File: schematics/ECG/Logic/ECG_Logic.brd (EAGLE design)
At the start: 29.6 x 27.7 mm, 77 parts, among them IC1 ADS1293, IC2 LIS3DH, IC3 MCP1703, IC4 CC2541, IC5 FSA4157, IC6 FSA4157, IC7 FSA4157, P1 TARGET_RA, P2 TARGET_RA, P3 TARGET_RA, P4 TARGET_RA, P5 TARGET_RA, P6 TARGET_RA, P7 TARGET_RA, X1 XTAL-2SMD, X2 XTAL_403, X3 ECS-40-20-4VX

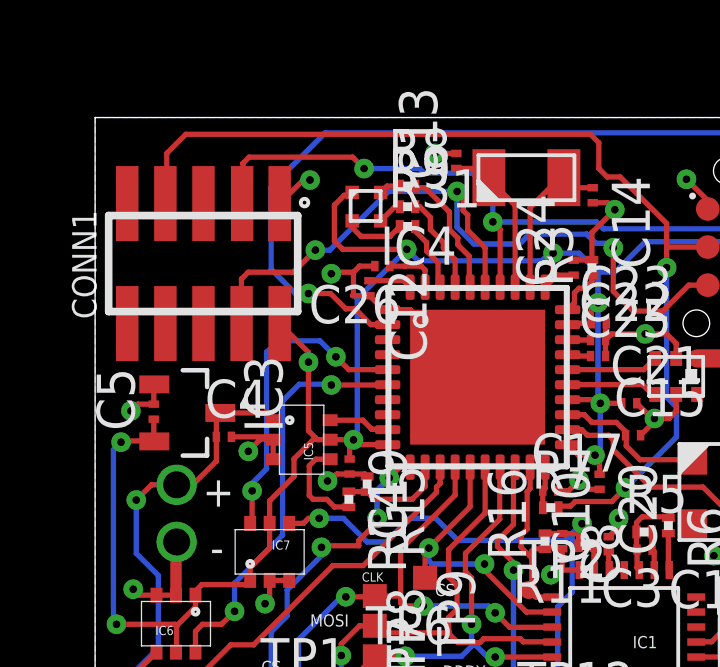
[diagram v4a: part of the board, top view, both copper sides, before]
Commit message: board only gets power when external accessory is plugged into it
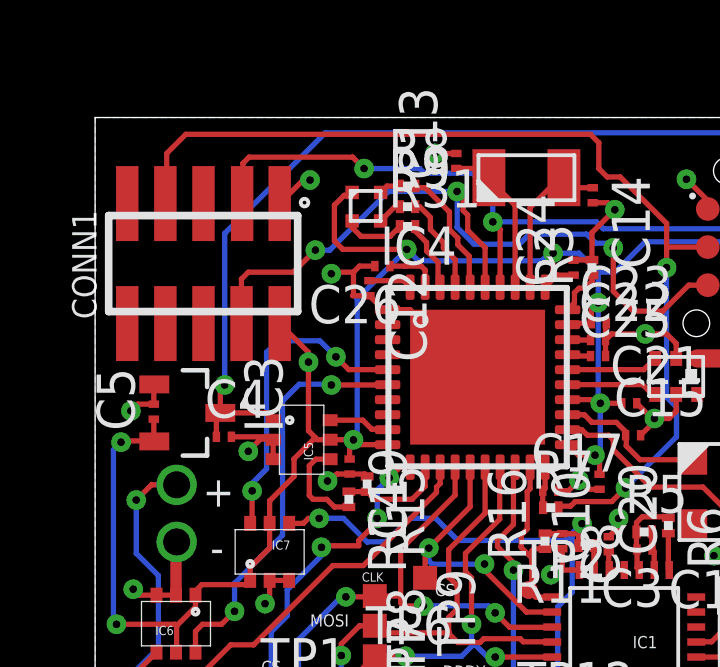
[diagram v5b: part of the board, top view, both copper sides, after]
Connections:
- removed net BOARD_DETECT: IC4.2, P7.1
- new net BATT_DETECT: C4.1, IC3.3, IC5.1, P7.1
- net BATT: no longer C4.1, IC3.3, IC5.1
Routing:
- net BATT_DETECT: track 0.00 -> 30.3 mm, vias 0 -> 1
- net BOARD_DETECT: track 26.8 -> 0.00 mm, vias 1 -> 0
- net BATT: track 44.2 -> 39.1 mm
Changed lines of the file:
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@@
 <?xml version="1.0" encoding="utf-8"?>
 <!DOCTYPE eagle SYSTEM "eagle.dtd">
-<eagle version="6.5.0">
+<eagle version="6.4">
 <drawing>
 <settings>
@@
 </signal>
 <signal name="BATT">
-<contactref element="IC5" pad="1"/>
-<contactref element="IC3" pad="3"/>
-<contactref element="C4" pad="1"/>
-<wire x1="4.1726" y1="17.8396" x2="5.6912" y2="17.8396" width="0.1778" layer="1"/>
-<wire x1="5.6912" y1="17.8396" x2="5.9338" y2="17.597" width="0.1778" layer="1"/>
-<wire x1="4.0426" y1="17.0434" x2="4.0426" y2="17.7096" width="0.1778" layer="1"/>
-<wire x1="4.0426" y1="17.7096" x2="4.1726" y2="17.8396" width="0.1778" layer="1"/>
-<wire x1="4.0426" y1="17.0434" x2="4.0426" y2="16.2346" width="0.1778" layer="1"/>
 <via x="1.3716" y="14.9352" extent="1-16" drill="0.254"/>
 <contactref element="P6" pad="1"/>
@@
 <wire x1="1.8796" y1="15.4432" x2="1.3716" y2="14.9352" width="0.1778" layer="1"/>
 <via x="2.7178" y="15.4432" extent="1-16" drill="0.9"/>
-<wire x1="2.7178" y1="15.4432" x2="1.8796" y2="15.4432" width="0.1778" layer="1"/>
-<wire x1="2.7178" y1="15.4432" x2="3.2512" y2="15.4432" width="0.1778" layer="1"/>
-<wire x1="3.2512" y1="15.4432" x2="4.0426" y2="16.2346" width="0.1778" layer="1"/>
 <wire x1="1.2446" y1="1.524" x2="1.9558" y2="0.8128" width="0.1778" layer="16"/>
 <wire x1="1.9558" y1="0.8128" x2="22.8346" y2="0.8128" width="0.1778" layer="16"/>
 <wire x1="22.8346" y1="0.8128" x2="23.9268" y2="1.905" width="0.1778" layer="16"/>
+<wire x1="1.8796" y1="15.4432" x2="2.7178" y2="15.4432" width="0.1778" layer="1"/>
 </signal>
 <signal name="BATT_CHECK_SW">
@@
 <contactref element="IC4" pad="3"/>
 </signal>
-<signal name="BOARD_DETECT">
-<contactref element="P7" pad="1"/>
-<contactref element="IC4" pad="2"/>
-<wire x1="9.7498" y1="20.7814" x2="9.1906" y2="20.7814" width="0.1778" layer="1"/>
-<wire x1="9.1906" y1="20.7814" x2="8.6614" y2="21.3106" width="0.1778" layer="1"/>
-<wire x1="8.6614" y1="21.3106" x2="8.3566" y2="21.3106" width="0.1778" layer="1"/>
-<wire x1="8.3566" y1="21.3106" x2="7.8486" y2="21.8186" width="0.1778" layer="1"/>
-<wire x1="7.8486" y1="21.8186" x2="7.112" y2="21.8186" width="0.1778" layer="1"/>
-<via x="7.112" y="21.8186" extent="1-16" drill="0.254"/>
-<wire x1="7.112" y1="21.8186" x2="6.6802" y2="21.8186" width="0.1778" layer="16"/>
-<wire x1="6.6802" y1="21.8186" x2="5.8674" y2="22.6314" width="0.1778" layer="16"/>
-<wire x1="5.8674" y1="22.6314" x2="5.8674" y2="25.3746" width="0.1778" layer="16"/>
-<wire x1="5.8674" y1="25.3746" x2="7.6708" y2="27.178" width="0.1778" layer="16"/>
-<wire x1="7.6708" y1="27.178" x2="22.1234" y2="27.178" width="0.1778" layer="16"/>
-<wire x1="23.5204" y1="25.781" x2="22.1234" y2="27.178" width="0.1778" layer="16"/>
-<wire x1="23.9268" y1="25.781" x2="23.5204" y2="25.781" width="0.1778" layer="16"/>
-</signal>
 <signal name="XTAL1">
 <contactref element="IC1" pad="23"/>
@@
 <wire x1="17.2172" y1="5.5793" x2="17.1323" y2="5.6642" width="0.1778" layer="1"/>
 </signal>
+<signal name="BATT_DETECT">
+<contactref element="IC3" pad="3"/>
+<contactref element="C4" pad="1"/>
+<wire x1="4.0426" y1="17.0434" x2="4.0426" y2="17.7096" width="0.1778" layer="1"/>
+<wire x1="4.0426" y1="17.7096" x2="4.1726" y2="17.8396" width="0.1778" layer="1"/>
+<contactref element="IC5" pad="1"/>
+<contactref element="P7" pad="1"/>
+<via x="4.318" y="18.7706" extent="1-16" drill="0.254"/>
+<wire x1="7.6708" y1="27.178" x2="22.1234" y2="27.178" width="0.1778" layer="16"/>
+<wire x1="23.5204" y1="25.781" x2="22.1234" y2="27.178" width="0.1778" layer="16"/>
+<wire x1="23.9268" y1="25.781" x2="23.5204" y2="25.781" width="0.1778" layer="16"/>
+<wire x1="4.318" y1="18.7706" x2="4.318" y2="23.8252" width="0.1778" layer="16"/>
+<wire x1="4.318" y1="23.8252" x2="7.6708" y2="27.178" width="0.1778" layer="16"/>
+<wire x1="4.1726" y1="17.8396" x2="4.1726" y2="18.6252" width="0.1778" layer="1"/>
+<wire x1="4.1726" y1="18.6252" x2="4.318" y2="18.7706" width="0.1778" layer="1"/>
+<wire x1="4.1726" y1="17.8396" x2="5.6912" y2="17.8396" width="0.1778" layer="1"/>
+<wire x1="5.6912" y1="17.8396" x2="5.9338" y2="17.597" width="0.1778" layer="1"/>
+</signal>
 </signals>

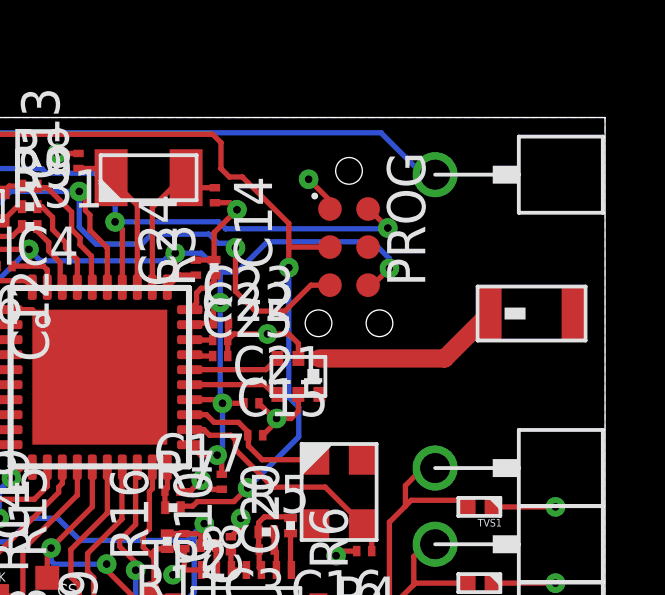
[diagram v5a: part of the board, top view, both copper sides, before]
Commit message: added 47uF cap to battery
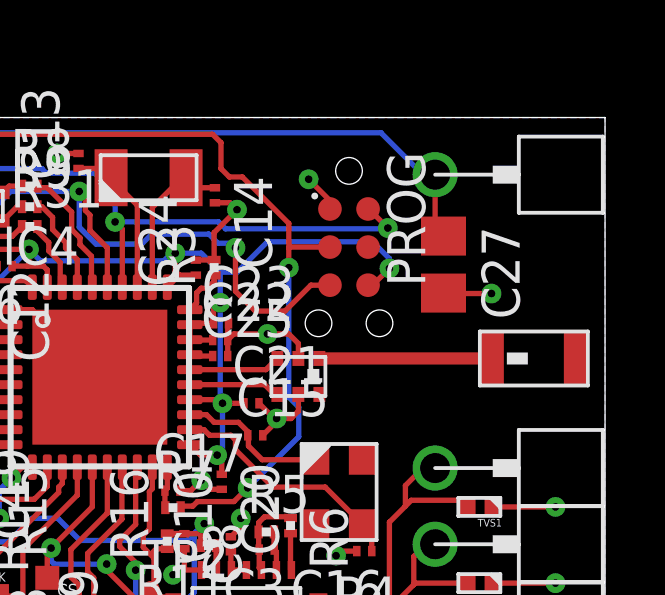
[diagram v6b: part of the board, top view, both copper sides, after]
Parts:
- added C27: (no value), rcl:C0805
- moved RF 1.50 mm to (27.3, 19.7)
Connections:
- net BATT_DETECT: now also C27.1
- net GND: now also C27.2
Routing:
- net BATT_DETECT: track 30.3 -> 32.5 mm
- net GND: track 60.9 -> 62.5 mm, vias 26 -> 27
- net N$6: track 6.29 -> 5.75 mm
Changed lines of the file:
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@@
 <?xml version="1.0" encoding="utf-8"?>
 <!DOCTYPE eagle SYSTEM "eagle.dtd">
-<eagle version="6.4">
+<eagle version="6.5.0">
 <drawing>
 <settings>
@@
 <element name="TVS3" library="semtech" package="0402" value="ZD_0402" x="25.4" y="9.6266" rot="R180"/>
 <element name="TVS4" library="semtech" package="0402" value="ZD_0402" x="25.4" y="7.0866" rot="R180"/>
-<element name="RF" library="johanson" package="ANTENNA_SMD" value="ANTENNA_SMD" x="27.218" y="21.1524" rot="R180"/>
+<element name="RF" library="johanson" package="ANTENNA_SMD" value="ANTENNA_SMD" x="27.2942" y="19.6538" rot="R180"/>
 <element name="IC8" library="johanson" package="BALUN_SMD_2450BM_SERIES" value="" x="19.304" y="19.0246"/>
 <element name="PROG" library="tagconnect" package="TC2030-MCP-NL" value="TC2030-MCP-NL" x="21.0566" y="25.908" rot="R270"/>
@@
 <element name="C1" library="rcl" package="C0201" value="20pF" x="12.4968" y="6.2103" rot="R90"/>
 <element name="C2" library="rcl" package="C0201" value="20pF" x="18.0975" y="5.8293" rot="R90"/>
+<element name="C27" library="rcl" package="C0805" value="" x="24.2062" y="22.7838" rot="R270"/>
 </elements>
 <signals>
@@
 <wire x1="25.8508" y1="12.1666" x2="27.94" y2="12.1666" width="0.1778" layer="1"/>
 <wire x1="25.8508" y1="14.7066" x2="27.94" y2="14.7066" width="0.1778" layer="1"/>
+<contactref element="C27" pad="2"/>
+<via x="25.8064" y="21.8186" extent="1-16" drill="0.254"/>
+<wire x1="25.8064" y1="21.8186" x2="24.2214" y2="21.8186" width="0.1778" layer="1"/>
+<wire x1="24.2214" y1="21.8186" x2="24.2062" y2="21.8338" width="0.1778" layer="1"/>
 </signal>
 <signal name="IN1">
@@
 <contactref element="IC8" pad="1"/>
 <contactref element="RF" pad="1"/>
-<wire x1="20.069" y1="19.6556" x2="24.2452" y2="19.6556" width="0.6096" layer="1"/>
-<wire x1="24.2452" y1="19.6556" x2="25.742" y2="21.1524" width="0.6096" layer="1"/>
+<wire x1="20.069" y1="19.6556" x2="25.8182" y2="19.6556" width="0.4064" layer="1"/>
+<wire x1="25.8182" y1="19.6556" x2="25.8182" y2="19.6538" width="0.4064" layer="1"/>
 </signal>
 <signal name="N/C">
@@
 <wire x1="4.1726" y1="17.8396" x2="5.6912" y2="17.8396" width="0.1778" layer="1"/>
 <wire x1="5.6912" y1="17.8396" x2="5.9338" y2="17.597" width="0.1778" layer="1"/>
+<contactref element="C27" pad="1"/>
+<wire x1="23.9268" y1="25.781" x2="23.9268" y2="24.0132" width="0.1778" layer="1"/>
+<wire x1="23.9268" y1="24.0132" x2="24.2062" y2="23.7338" width="0.1778" layer="1"/>
 </signal>
 </signals>

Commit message: removed board comments that are no long applicable. Added missing values to scheamtic components
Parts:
- C27: value (none) -> 47uF
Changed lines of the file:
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@@
 <element name="C1" library="rcl" package="C0201" value="20pF" x="12.4968" y="6.2103" rot="R90"/>
 <element name="C2" library="rcl" package="C0201" value="20pF" x="18.0975" y="5.8293" rot="R90"/>
-<element name="C27" library="rcl" package="C0805" value="" x="24.2062" y="22.7838" rot="R270"/>
+<element name="C27" library="rcl" package="C0805" value="47uF" x="24.2062" y="22.7838" rot="R270"/>
 </elements>
 <signals>

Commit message: removed unused scheamtic trace, updated BOM
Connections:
- removed net OSC_SW_VCC: IC4.3
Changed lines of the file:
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@@
 <?xml version="1.0" encoding="utf-8"?>
 <!DOCTYPE eagle SYSTEM "eagle.dtd">
-<eagle version="6.5.0">
+<eagle version="6.4">
 <drawing>
 <settings>
@@
 <contactref element="IC4" pad="4"/>
 </signal>
-<signal name="OSC_SW_VCC">
-<contactref element="IC4" pad="3"/>
-</signal>
 <signal name="XTAL1">
